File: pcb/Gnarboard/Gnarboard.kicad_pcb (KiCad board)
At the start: 2 copper layers, 155 x 124 mm, 114 parts, among them J10 Screw_Terminal_01x02, J11 Screw_Terminal_01x02, J12 Screw_Terminal_01x02, J3 Screw_Terminal_01x12, J4 Screw_Terminal_01x12, J5 Screw_Terminal_01x02, J6 Screw_Terminal_01x02, J7 Screw_Terminal_01x02, J8 Screw_Terminal_01x02, J9 Screw_Terminal_01x02, Q1 MMBT5551L, Q10 IRF4905, Q11 MMBT5551L, Q12 IRF4905, Q13 MMBT5551L, Q14 IRF4905, Q15 MMBT5551L, Q16 IRF4905, Q2 IRF4905, Q3 MMBT5551L, Q4 IRF4905, Q5 MMBT5551L, Q6 IRF4905, Q7 MMBT5551L, Q8 IRF4905, Q9 MMBT5551L, U10 ACS725xLCTR-20AU, U11 ACS725xLCTR-20AU, U12 ACS725xLCTR-20AU, U2 MCP3208, U4 D24V5F3, U5 ACS725xLCTR-20AU, U6 ACS725xLCTR-20AU, U7 ACS725xLCTR-20AU, U8 ACS725xLCTR-20AU, U9 ACS725xLCTR-20AU

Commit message: added the flyback diode
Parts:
- added D10: GS1G-LTP, Diode_SMD:D_SMA, F.Cu at (98.8, 124.0)
- added D11: GS1G-LTP, Diode_SMD:D_SMA, F.Cu at (113.8, 124.0)
- added D12: GS1G-LTP, Diode_SMD:D_SMA, F.Cu at (128.8, 124.0)
- added D13: GS1G-LTP, Diode_SMD:D_SMA, F.Cu at (143.8, 123.9)
- added D14: GS1G-LTP, Diode_SMD:D_SMA, F.Cu at (158.8, 124.0)
- added D15: GS1G-LTP, Diode_SMD:D_SMA, F.Cu at (173.8, 124.0)
- added D16: GS1G-LTP, Diode_SMD:D_SMA, F.Cu at (188.8, 124.0)
- added D17: GS1G-LTP, Diode_SMD:D_SMA, F.Cu at (203.8, 124.0)
- R11, R15, R19, R23, R27, R3, R31, R7: value 10k -> 47k
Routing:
- net +24V: track 706.2 -> 739.3 mm
- net Net-(D12-K): track 71.9 -> 82.0 mm
- net Net-(D17-K): track 71.9 -> 82.0 mm
- net Net-(D11-K): track 71.9 -> 82.0 mm
- net Net-(D16-K): track 71.9 -> 82.0 mm
- net Net-(D14-K): track 71.9 -> 82.0 mm
- net Net-(D15-K): track 71.9 -> 82.0 mm
- net Net-(D13-K): track 71.9 -> 82.0 mm
- net Net-(D12-A): track 7.15 -> 0.00 mm
- net Net-(D11-A): track 7.15 -> 0.00 mm
- net Net-(D10-A): track 7.15 -> 0.00 mm
- net Net-(D17-A): track 7.15 -> 0.00 mm
- net Net-(D16-A): track 7.15 -> 0.00 mm
- net Net-(D15-A): track 7.15 -> 0.00 mm
- net Net-(D14-A): track 7.15 -> 0.00 mm
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
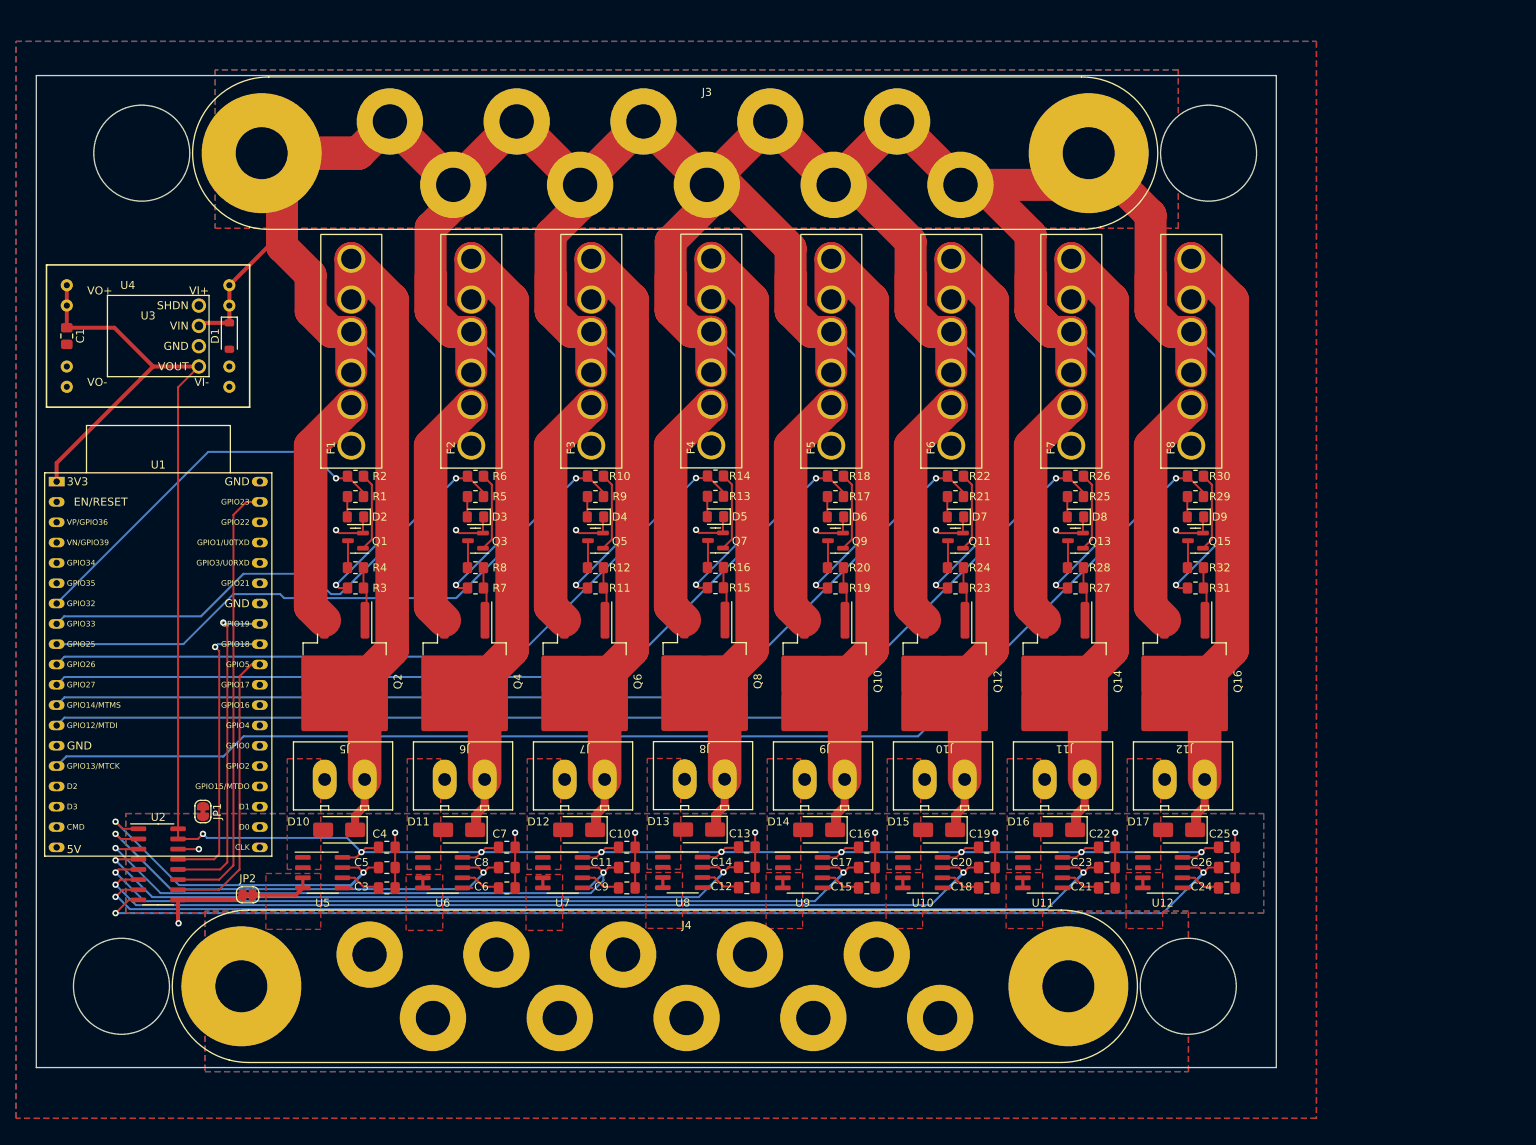
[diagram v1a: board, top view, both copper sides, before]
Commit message: added a qwiic connector
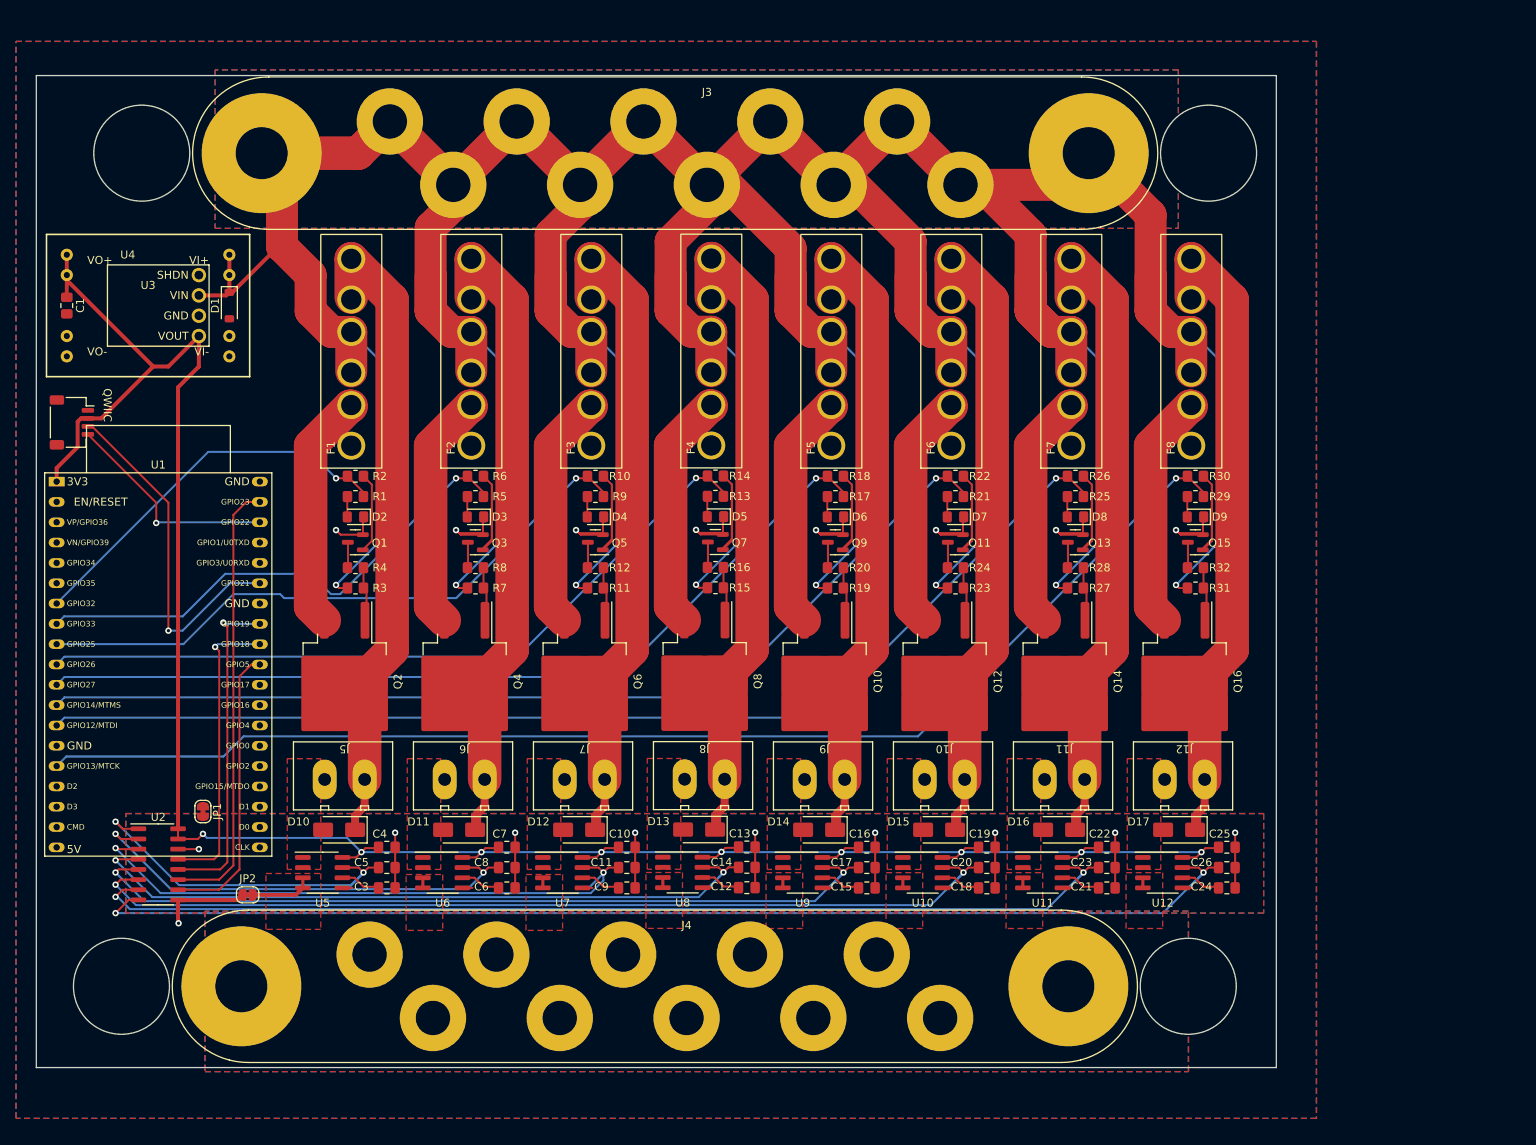
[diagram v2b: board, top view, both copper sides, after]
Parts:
- added QWIIC: I2C, Connector_JST:JST_SH_SM04B-SRSS-TB_1x04-1MP_P1.00mm_Horizontal, F.Cu at (65.4, 73.0)
- moved C1 3.81 mm to (64.8, 58.4)
- moved D1 3.81 mm to (85.1, 58.4)
- moved U3 3.81 mm to (74.9, 58.4)
- moved U4 3.81 mm to (77.5, 58.4)
- moved Q11 0.20 mm to (175.8, 88.0)
- moved Q13 0.20 mm to (190.8, 88.0)
- moved Q15 0.20 mm to (205.8, 88.0)
- moved Q5 0.20 mm to (130.8, 88.0)
- moved Q7 0.20 mm to (145.8, 88.0)
- moved Q9 0.20 mm to (160.8, 88.0)
- moved Q1 0.20 mm to (100.8, 88.0)
- moved Q3 0.20 mm to (115.8, 88.0)
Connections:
- U1 pad 33: unconnected-(U1-GPIO21-Pad33) -> SDA
- U1 pad 36: unconnected-(U1-GPIO22-Pad36) -> SCL
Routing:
- net SDA: track 0.00 -> 43.9 mm, vias 0 -> 1
- net GNDD: track 54.9 -> 95.3 mm
- net SCL: track 0.00 -> 27.6 mm, vias 0 -> 1
- net +3.3V: track 271.5 -> 281.5 mm
- net Net-(Q9-B): track 9.90 -> 18.5 mm
- net Net-(Q7-B): track 9.90 -> 18.5 mm
- net Net-(Q5-B): track 9.90 -> 18.5 mm
- net Net-(Q3-B): track 9.90 -> 18.5 mm
- net Net-(Q15-B): track 9.90 -> 18.5 mm
- net Net-(Q11-B): track 9.90 -> 18.5 mm
- net Net-(Q13-B): track 9.90 -> 18.5 mm
- net Net-(Q9-C): track 3.31 -> 6.43 mm
- net Net-(Q7-C): track 3.31 -> 6.43 mm
- net Net-(Q5-C): track 3.31 -> 6.43 mm
- net Net-(Q15-C): track 3.31 -> 6.43 mm
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
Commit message: bill of materials updated.
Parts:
- removed QWIIC: I2C, Connector_JST:JST_SH_SM04B-SRSS-TB_1x04-1MP_P1.00mm_Horizontal
- removed U3: ~, gnarboard:DF1768
- added DFR0570: ~, gnarboard:DF1768, F.Cu at (74.9, 58.4)
- added J2: I2C, Connector_JST:JST_SH_SM04B-SRSS-TB_1x04-1MP_P1.00mm_Horizontal, F.Cu at (65.4, 73.0)
- U1: value ~ -> ESP32-DEVKITC

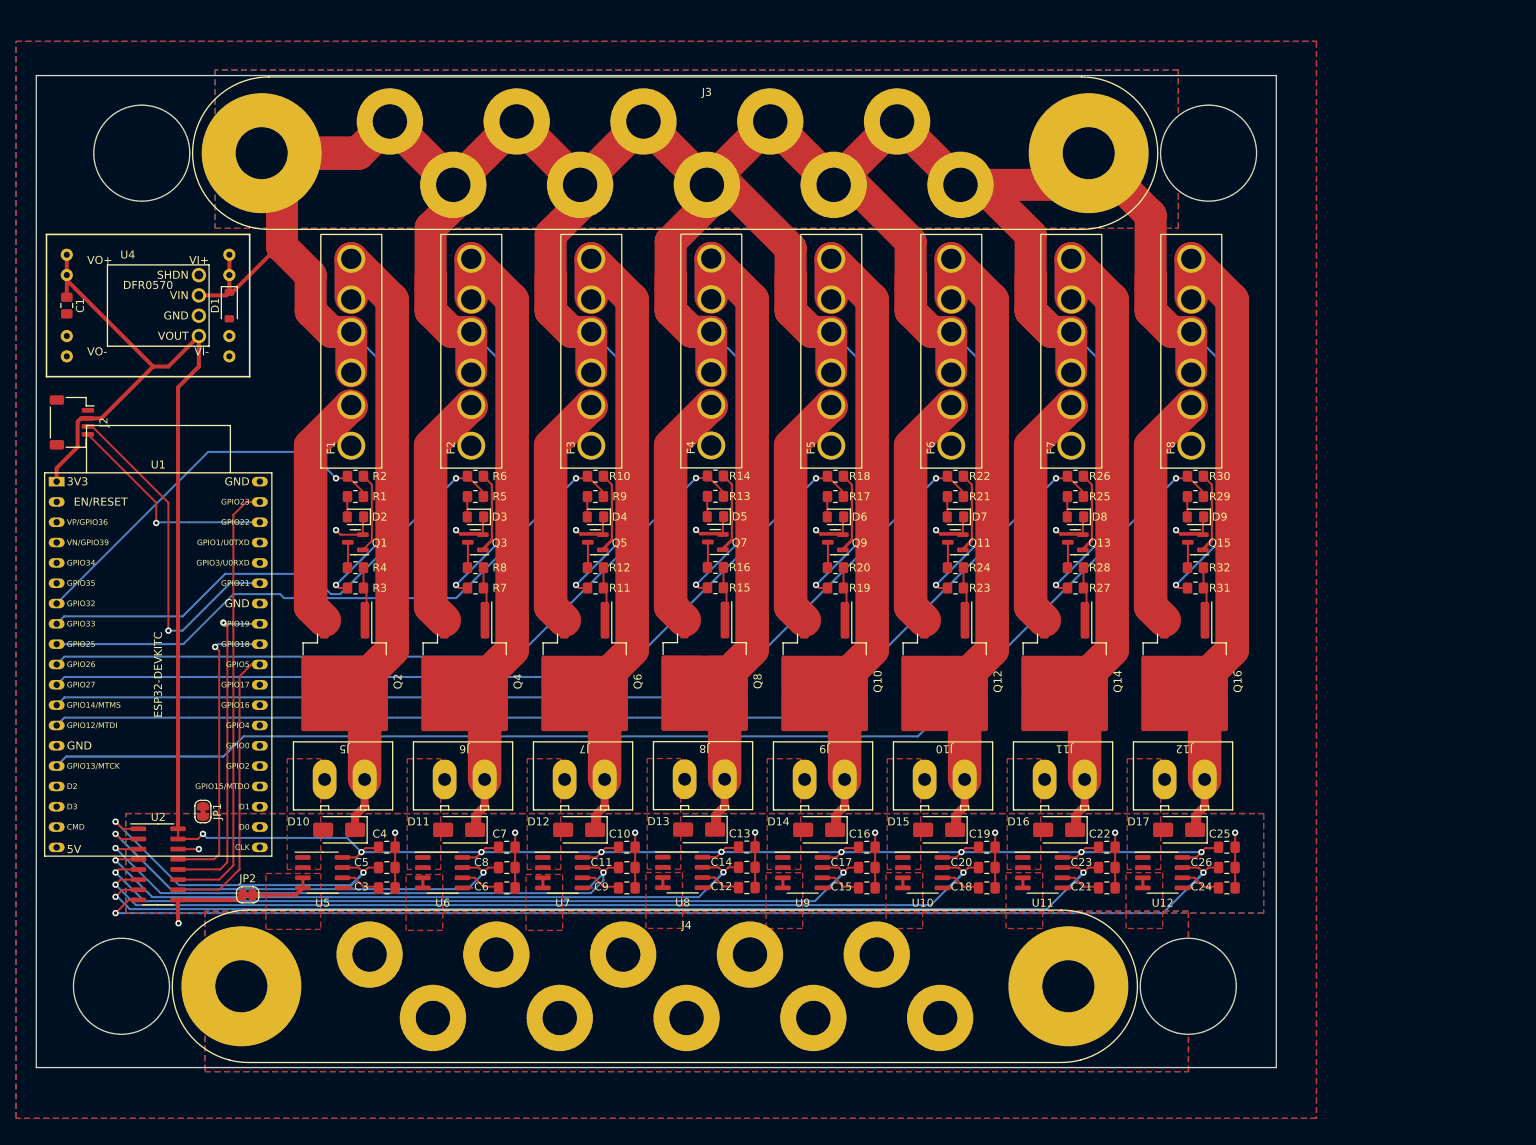
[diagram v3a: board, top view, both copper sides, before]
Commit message: got the mosfet driver circuit sorted - zener to the rescue.  also added the CAN/N2K header.
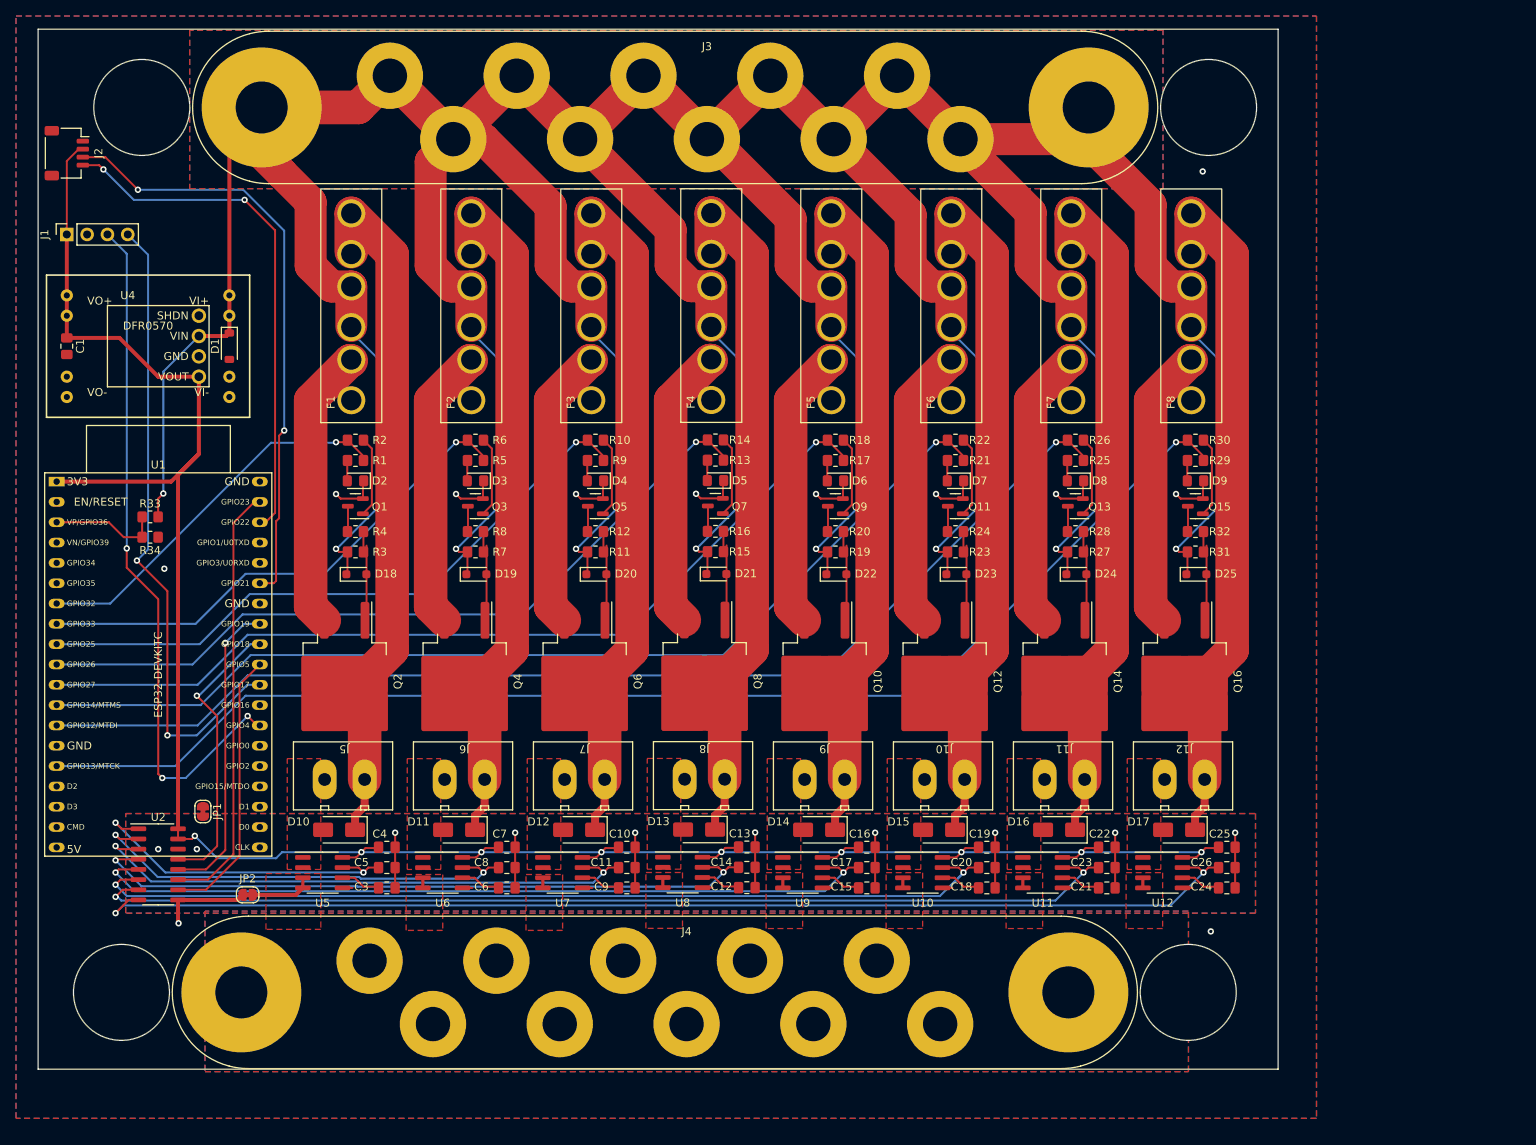
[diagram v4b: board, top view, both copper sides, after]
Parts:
- added D18: 15V, Diode_SMD:D_SOD-323_HandSoldering, F.Cu at (101.0, 92.0)
- added D19: 15V, Diode_SMD:D_SOD-323_HandSoldering, F.Cu at (116.0, 92.0)
- added D20: 15V, Diode_SMD:D_SOD-323_HandSoldering, F.Cu at (131.0, 92.0)
- added D21: 15V, Diode_SMD:D_SOD-323_HandSoldering, F.Cu at (146.0, 92.0)
- added D22: 15V, Diode_SMD:D_SOD-323_HandSoldering, F.Cu at (161.0, 92.0)
- added D23: 15V, Diode_SMD:D_SOD-323_HandSoldering, F.Cu at (176.0, 92.0)
- added D24: 15V, Diode_SMD:D_SOD-323_HandSoldering, F.Cu at (191.0, 92.0)
- added D25: 15V, Diode_SMD:D_SOD-323_HandSoldering, F.Cu at (206.0, 92.0)
- added J1: N2K, Connector_PinSocket_2.54mm:PinSocket_1x04_P2.54mm_Vertical, F.Cu at (64.8, 49.5)
- added R33: 100k, Resistor_SMD:R_0805_2012Metric_Pad1.20x1.40mm_HandSolder, F.Cu at (75.2, 84.8)
- added R34: 10k, Resistor_SMD:R_0805_2012Metric_Pad1.20x1.40mm_HandSolder, F.Cu at (75.2, 87.4)
- R11, R15, R19, R23, R27, R3, R31, R7: value 47k -> 33k
- R12, R16, R20, R24, R28, R32, R4, R8: value 100k -> 6.8k
- moved J2 33.7 mm to (64.8, 39.4)
- moved J3 5.71 mm to (144.8, 33.7)
- moved F1 5.68 mm to (100.3, 59.1)
- moved F2 5.68 mm to (115.3, 59.1)
- moved F3 5.68 mm to (130.3, 59.1)
- moved F4 5.68 mm to (145.3, 59.1)
- moved F5 5.68 mm to (160.3, 59.1)
- moved F6 5.68 mm to (175.3, 59.1)
- moved F7 5.68 mm to (190.3, 59.1)
- moved F8 5.68 mm to (205.3, 59.1)
- moved C1 5.08 mm to (64.8, 63.5)
- moved D1 5.08 mm to (85.1, 63.5)
- moved DFR0570 5.08 mm to (74.9, 63.5)
- moved U4 5.08 mm to (77.5, 63.5)
- moved R1 4.51 mm to (100.9, 77.8)
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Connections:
- U1 pad 26: unconnected-(U1-GPIO4-Pad26) -> CAN_RX
- U1 pad 28: unconnected-(U1-GPIO17-Pad28) -> CAN_TX
- U1 pad 3: unconnected-(U1-GPIO36-Pad3) -> Net-(U1-GPIO36)
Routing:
- net CAN_RX: track 0.00 -> 86.7 mm, vias 0 -> 3
- net CAN_TX: track 0.00 -> 80.0 mm, vias 0 -> 2
- net GNDD: track 95.3 -> 57.1 mm, vias 9 -> 12
- net SCL: track 27.6 -> 65.1 mm, vias 1 -> 2
- net SDA: track 43.9 -> 75.3 mm, vias 1 -> 2
- net Net-(U1-GPIO36): track 0.00 -> 14.0 mm
- net +3.3V: track 281.5 -> 290.0 mm
- net Net-(Q3-B): track 18.5 -> 10.1 mm
- net Net-(Q9-B): track 18.5 -> 10.1 mm
- net Net-(Q7-B): track 18.5 -> 10.1 mm
- net Net-(Q5-B): track 18.5 -> 10.1 mm
- net Net-(Q15-B): track 18.5 -> 10.1 mm
- net Net-(Q11-B): track 18.5 -> 10.1 mm
- net Net-(Q13-B): track 18.5 -> 10.1 mm
- net +24V: track 740.5 -> 733.5 mm, vias 8 -> 9
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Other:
- board size 155 x 124 mm -> 155 x 130 mm
